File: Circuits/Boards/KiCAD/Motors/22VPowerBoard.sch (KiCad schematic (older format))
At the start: 13 parts, among them J1 Conn_01x01, J2 Conn_01x01, J3 Conn_01x01, U1 HCPL063

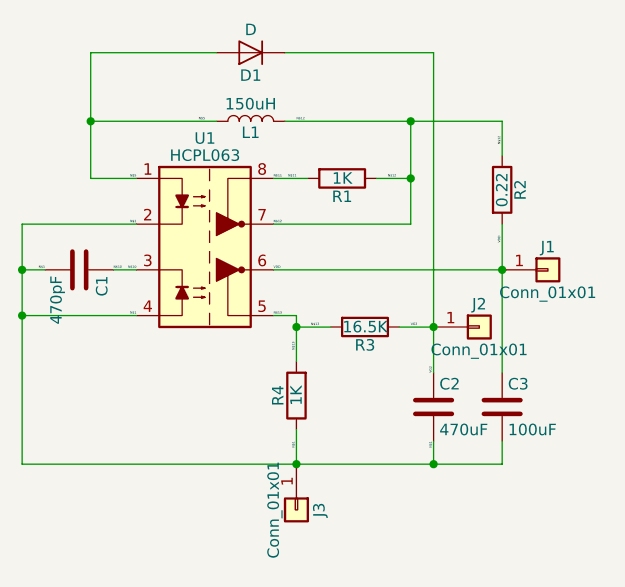
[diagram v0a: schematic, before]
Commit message: Update KiCAD motor controller and Version 2 simulation
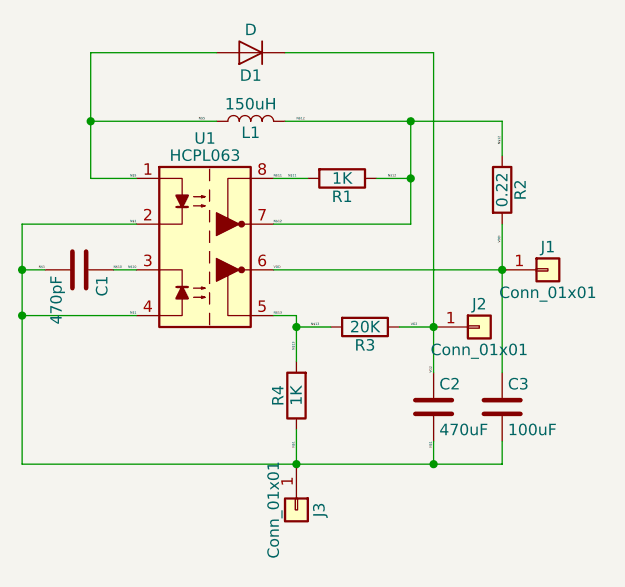
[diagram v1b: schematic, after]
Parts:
- R3: value 16.5K -> 20K
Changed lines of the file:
@@
 P 11200 7800
 F 0 "R3" V 11280 7800 50  0000 C CNN
-F 1 "16.5K" V 11200 7800 50  0000 C CNN
+F 1 "20K" V 11200 7800 50  0000 C CNN
 F 2 "Resistors_THT:R_Axial_DIN0207_L6.3mm_D2.5mm_P2.54mm_Vertical" V 11130 7800 50  0001 C CNN
 F 3 "" H 11200 7800 50  0001 C CNN
